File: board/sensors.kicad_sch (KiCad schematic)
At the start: 59 parts, among them J4 SWIM, U4 STM8S003F3P, U5 MAX-M8C, U6 LM324, U7 LM324

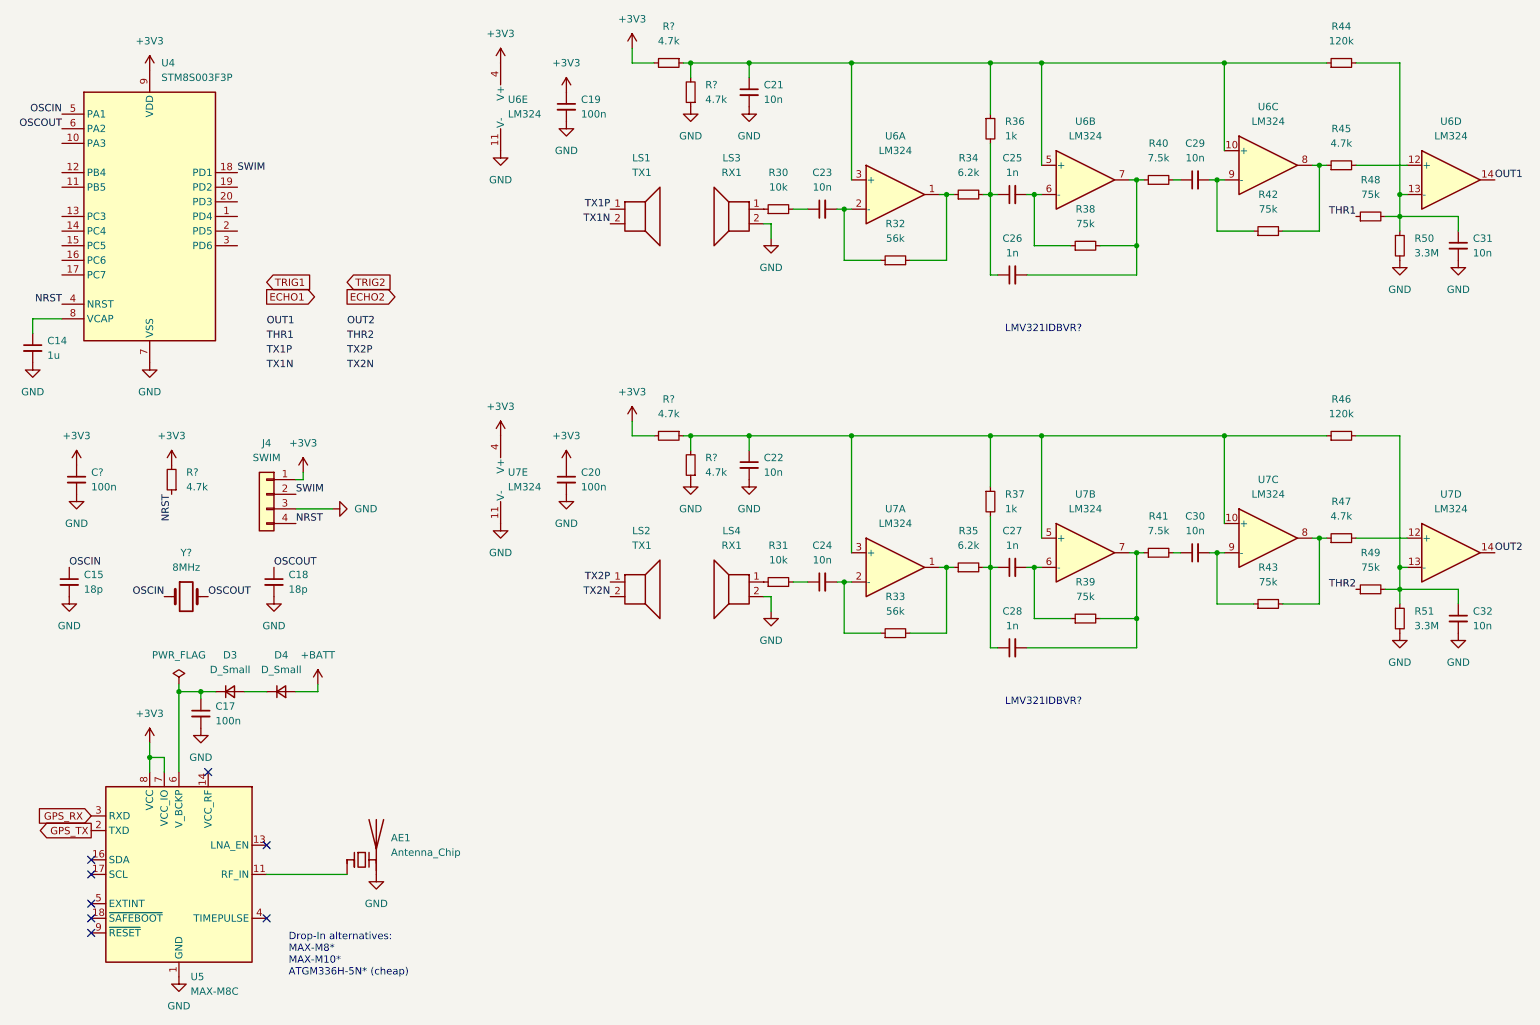
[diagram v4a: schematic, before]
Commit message: Added new ultrasonic circuit, changed the 3.3V regulator to a buck converter, and fixed some issues
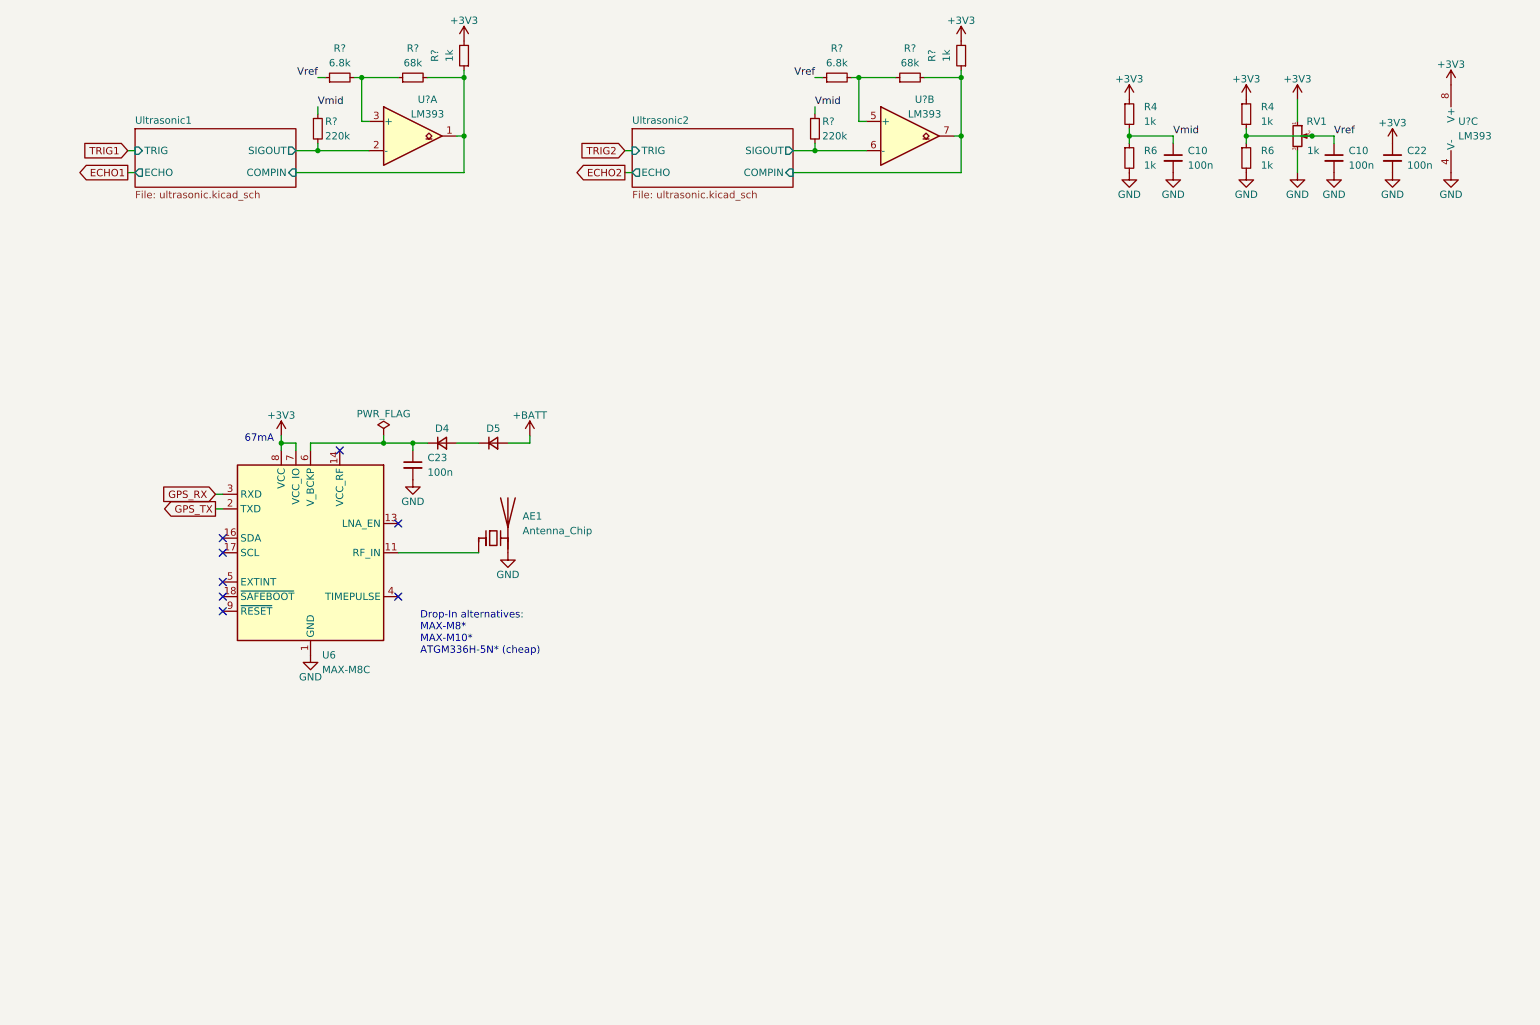
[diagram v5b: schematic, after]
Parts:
- removed C14: 1u, Capacitor_SMD:C_0603_1608Metric, symbol Device:C_Small
- removed C15, C18: 18p, Capacitor_SMD:C_0603_1608Metric, symbol Device:C_Small
- removed C19, C20, C?: 100n, Capacitor_SMD:C_0603_1608Metric, symbol Device:C_Small
- removed C21, C23, C24, C29, C30, C31, C32: 10n, Capacitor_SMD:C_0603_1608Metric, symbol Device:C_Small
- removed C25, C26, C27, C28: 1n, Capacitor_SMD:C_0603_1608Metric, symbol Device:C_Small
- removed J4: SWIM, symbol Connector_Generic:Conn_01x04
- removed LS1, LS2: TX1, symbol Device:Speaker
- removed LS3, LS4: RX1, symbol Device:Speaker
- removed R30, R31: 10k, Resistor_SMD:R_0603_1608Metric, symbol Device:R_Small
- removed R32, R33: 56k, Resistor_SMD:R_0603_1608Metric, symbol Device:R_Small
- removed R34, R35: 6.2k, Resistor_SMD:R_0603_1608Metric, symbol Device:R_Small
- removed R36, R37: 1k, Resistor_SMD:R_0603_1608Metric, symbol Device:R_Small
- removed R38, R39, R42, R43, R48, R49: 75k, Resistor_SMD:R_0603_1608Metric, symbol Device:R_Small
- removed R40, R41: 7.5k, Resistor_SMD:R_0603_1608Metric, symbol Device:R_Small
- removed R44, R46: 120k, Resistor_SMD:R_0603_1608Metric, symbol Device:R_Small
- removed R45, R47, R? (x5): 4.7k, Resistor_SMD:R_0603_1608Metric, symbol Device:R_Small
- removed R50, R51: 3.3M, Resistor_SMD:R_0603_1608Metric, symbol Device:R_Small
- removed U4: STM8S003F3P, Package_SO:TSSOP-20_4.4x6.5mm_P0.65mm, symbol MCU_ST_STM8:STM8S003F3P
- removed U6, U7: LM324, Package_SO:SOIC-14_3.9x8.7mm_P1.27mm, symbol Amplifier_Operational:LM324
- removed Y?: Crystal, symbol Device:Crystal
- added C10 (x2): 100n, Capacitor_SMD:C_0603_1608Metric_Pad1.08x0.95mm_HandSolder, symbol Device:C_Small
- added R4 (x2), R6 (x2), R? (x2): 1k, Resistor_SMD:R_0603_1608Metric, symbol Device:R_Small
- added R? (x2): 75k, Resistor_SMD:R_0603_1608Metric, symbol Device:R_Small
- added R? (x2): R_Small, Resistor_SMD:R_0603_1608Metric, symbol Device:R_Small
- added R? (x2): 3.3M, Resistor_SMD:R_0603_1608Metric, symbol Device:R_Small
- added RV1: 1k, Potentiometer_THT:Potentiometer_Bourns_3266W_Vertical, symbol Device:R_Potentiometer_Small
- added U? (x3): LM393, Package_SO:SOIC-8_3.9x4.9mm_P1.27mm, symbol Comparator:LM393
- AE1: footprint (none) -> OBSPro:GPS1003
- C22: value 10n -> 100n; footprint Capacitor_SMD:C_0603_1608Metric -> Capacitor_SMD:C_0603_1608Metric_Pad1.08x0.95mm_HandSolder; JLC_PN C57112 -> C14663; JLC_Price1 (none) -> 0.042; JLC_Price10 (none) -> 0.0042; JLC_Price100 (none) -> 0.0021; JLC_Price1000 (none) -> 0.0014; MPN 0603B103K500NT -> CC0603KRX7R9BB104; Manufacturer FH (Guangdong Fenghua Advanced Tech) -> YAGEO; kicost:JLC:pricing 1: USD 0.0012 -> (none)
- renumbered C17 to C23, D3 to D4, D4 to D5, U5 to U6
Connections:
- net +3V3: now also C22.1, R4.1, R4.1, R?.2, R?.2, RV1.1, U?.8 (V+)
- net GND: now also C10.2, C10.2, R6.2, R6.2, RV1.3, U?.4 (V-)
- new net: R?.1, R?.2, U?.5 (+)
- new net: R?.1, R?.2, U?.3 (+)
- new net Ultrasonic1/COMPIN: R?.1, R?.2, U?.1
- new net Ultrasonic1/SIGOUT: R?.2, U?.2 (-)
- new net Ultrasonic2/COMPIN: R?.1, R?.2, U?.7
- new net Ultrasonic2/SIGOUT: R?.2, U?.6 (-)
- new net Vmid: C10.1, R4.2, R6.1, R?.1, R?.1
- new net Vref: C10.1, R4.2, R6.1, R?.1, R?.1, RV1.2
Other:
- added sheet Ultrasonic1 (ultrasonic.kicad_sch)
- added sheet Ultrasonic2 (ultrasonic.kicad_sch)
- note added: "67mA"
- note removed: "LMV321IDBVR?"
- moved on the sheet: AE1, C23, D4, D5, U6

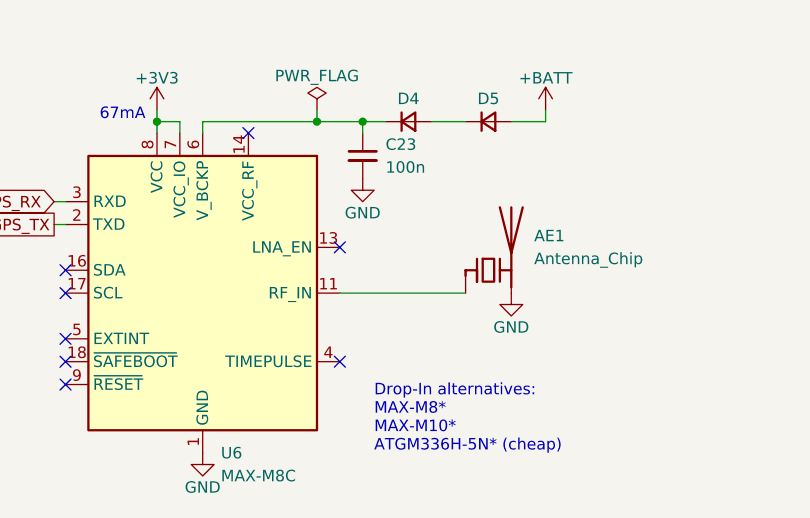
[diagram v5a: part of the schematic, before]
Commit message: First placement of parts, fixed a few bugs in the schematic
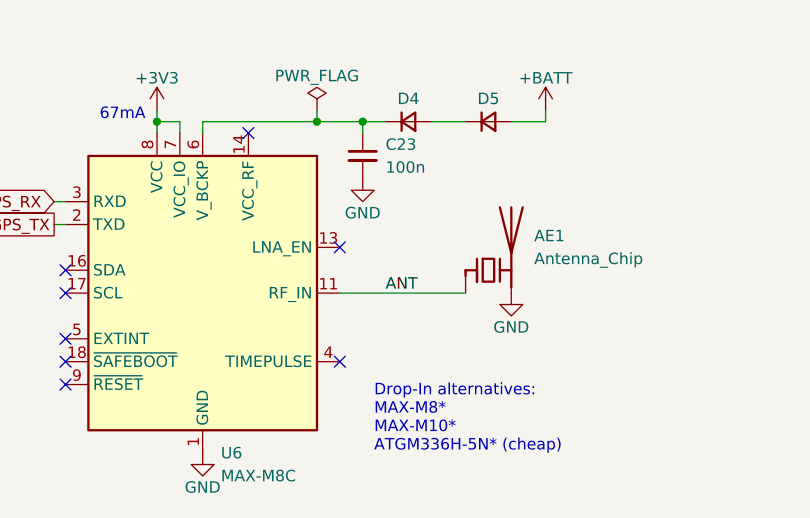
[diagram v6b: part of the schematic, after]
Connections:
- net ANT: now reaches AE1.1 (FEED), U6.11 (RF_IN)
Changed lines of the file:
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@@
+    (effects (font (size 1.27 1.27)) (justify left bottom))
+  )
+  (label "ANT" (at 87.63 115.57 0)
     (effects (font (size 1.27 1.27)) (justify left bottom))
   )
@@
   (symbol (lib_id "power:GND") (at 85.09 102.87 0) (unit 1)
     (in_bom yes) (on_board yes) (fields_autoplaced)
-    (property "Reference" "#PWR0152" (id 0) (at 85.09 109.22 0)
+    (property "Reference" "#PWR082" (id 0) (at 85.09 109.22 0)
       (effects (font (size 1.27 1.27)) hide)
     )
@@
   (symbol (lib_id "power:+3V3") (at 93.98 26.67 0) (unit 1)
     (in_bom yes) (on_board yes) (fields_autoplaced)
-    (property "Reference" "#PWR0201" (id 0) (at 93.98 30.48 0)
+    (property "Reference" "#PWR066" (id 0) (at 93.98 30.48 0)
       (effects (font (size 1.27 1.27)) hide)
     )
@@
   (symbol (lib_id "power:+3V3") (at 238.76 36.83 0) (unit 1)
     (in_bom yes) (on_board yes) (fields_autoplaced)
-    (property "Reference" "#PWR0205" (id 0) (at 238.76 40.64 0)
+    (property "Reference" "#PWR071" (id 0) (at 238.76 40.64 0)
       (effects (font (size 1.27 1.27)) hide)
     )
@@
   (symbol (lib_id "power:GND") (at 265.43 49.53 0) (unit 1)
     (in_bom yes) (on_board yes) (fields_autoplaced)
-    (property "Reference" "#PWR0159" (id 0) (at 265.43 55.88 0)
+    (property "Reference" "#PWR079" (id 0) (at 265.43 55.88 0)
       (effects (font (size 1.27 1.27)) hide)
     )
@@
   (symbol (lib_id "power:GND") (at 238.76 49.53 0) (unit 1)
     (in_bom yes) (on_board yes) (fields_autoplaced)
-    (property "Reference" "#PWR0157" (id 0) (at 238.76 55.88 0)
+    (property "Reference" "#PWR076" (id 0) (at 238.76 55.88 0)
       (effects (font (size 1.27 1.27)) hide)
     )
@@
   (symbol (lib_id "power:+3V3") (at 255.27 44.45 0) (unit 1)
     (in_bom yes) (on_board yes) (fields_autoplaced)
-    (property "Reference" "#PWR0225" (id 0) (at 255.27 48.26 0)
+    (property "Reference" "#PWR072" (id 0) (at 255.27 48.26 0)
       (effects (font (size 1.27 1.27)) hide)
     )
@@
   (symbol (lib_id "power:GND") (at 229.87 49.53 0) (unit 1)
     (in_bom yes) (on_board yes) (fields_autoplaced)
-    (property "Reference" "#PWR0156" (id 0) (at 229.87 55.88 0)
+    (property "Reference" "#PWR075" (id 0) (at 229.87 55.88 0)
       (effects (font (size 1.27 1.27)) hide)
     )
@@
   (symbol (lib_id "power:+3V3") (at 62.23 95.25 0) (unit 1)
     (in_bom yes) (on_board yes) (fields_autoplaced)
-    (property "Reference" "#PWR0203" (id 0) (at 62.23 99.06 0)
+    (property "Reference" "#PWR080" (id 0) (at 62.23 99.06 0)
       (effects (font (size 1.27 1.27)) hide)
     )
@@
   (symbol (lib_id "power:GND") (at 67.31 133.35 0) (unit 1)
     (in_bom yes) (on_board yes) (fields_autoplaced)
-    (property "Reference" "#PWR0151" (id 0) (at 67.31 139.7 0)
+    (property "Reference" "#PWR084" (id 0) (at 67.31 139.7 0)
       (effects (font (size 1.27 1.27)) hide)
     )
@@
   (symbol (lib_id "power:GND") (at 255.27 49.53 0) (unit 1)
     (in_bom yes) (on_board yes) (fields_autoplaced)
-    (property "Reference" "#PWR0158" (id 0) (at 255.27 55.88 0)
+    (property "Reference" "#PWR078" (id 0) (at 255.27 55.88 0)
       (effects (font (size 1.27 1.27)) hide)
     )
@@
   (symbol (lib_id "power:GND") (at 101.6 115.57 0) (unit 1)
     (in_bom yes) (on_board yes) (fields_autoplaced)
-    (property "Reference" "#PWR0153" (id 0) (at 101.6 121.92 0)
+    (property "Reference" "#PWR083" (id 0) (at 101.6 121.92 0)
       (effects (font (size 1.27 1.27)) hide)
     )
@@
   (symbol (lib_id "power:GND") (at 217.17 49.53 0) (unit 1)
     (in_bom yes) (on_board yes) (fields_autoplaced)
-    (property "Reference" "#PWR0155" (id 0) (at 217.17 55.88 0)
+    (property "Reference" "#PWR074" (id 0) (at 217.17 55.88 0)
       (effects (font (size 1.27 1.27)) hide)
     )
@@
   (symbol (lib_id "power:+3V3") (at 229.87 36.83 0) (unit 1)
     (in_bom yes) (on_board yes) (fields_autoplaced)
-    (property "Reference" "#PWR0206" (id 0) (at 229.87 40.64 0)
+    (property "Reference" "#PWR070" (id 0) (at 229.87 40.64 0)
       (effects (font (size 1.27 1.27)) hide)
     )
@@
   (symbol (lib_id "power:GND") (at 245.11 49.53 0) (unit 1)
     (in_bom yes) (on_board yes) (fields_autoplaced)
-    (property "Reference" "#PWR0160" (id 0) (at 245.11 55.88 0)
+    (property "Reference" "#PWR077" (id 0) (at 245.11 55.88 0)
       (effects (font (size 1.27 1.27)) hide)
     )
@@
   (symbol (lib_id "power:+BATT") (at 105.41 95.25 0) (unit 1)
     (in_bom yes) (on_board yes) (fields_autoplaced)
-    (property "Reference" "#PWR0204" (id 0) (at 105.41 99.06 0)
+    (property "Reference" "#PWR081" (id 0) (at 105.41 99.06 0)
       (effects (font (size 1.27 1.27)) hide)
     )
@@
   (symbol (lib_id "power:+3V3") (at 180.34 26.67 0) (unit 1)
     (in_bom yes) (on_board yes) (fields_autoplaced)
-    (property "Reference" "#PWR0202" (id 0) (at 180.34 30.48 0)
+    (property "Reference" "#PWR067" (id 0) (at 180.34 30.48 0)
       (effects (font (size 1.27 1.27)) hide)
     )
@@
   (symbol (lib_id "power:+3V3") (at 265.43 34.29 0) (unit 1)
     (in_bom yes) (on_board yes) (fields_autoplaced)
-    (property "Reference" "#PWR0208" (id 0) (at 265.43 38.1 0)
+    (property "Reference" "#PWR068" (id 0) (at 265.43 38.1 0)
       (effects (font (size 1.27 1.27)) hide)
     )
@@
   (symbol (lib_id "power:GND") (at 209.55 49.53 0) (unit 1)
     (in_bom yes) (on_board yes) (fields_autoplaced)
-    (property "Reference" "#PWR0154" (id 0) (at 209.55 55.88 0)
+    (property "Reference" "#PWR073" (id 0) (at 209.55 55.88 0)
       (effects (font (size 1.27 1.27)) hide)
     )
@@
   (symbol (lib_id "power:+3V3") (at 209.55 36.83 0) (unit 1)
     (in_bom yes) (on_board yes) (fields_autoplaced)
-    (property "Reference" "#PWR0207" (id 0) (at 209.55 40.64 0)
+    (property "Reference" "#PWR069" (id 0) (at 209.55 40.64 0)
       (effects (font (size 1.27 1.27)) hide)
     )
@@
   (symbol (lib_id "power:PWR_FLAG") (at 80.01 95.25 0) (unit 1)
     (in_bom yes) (on_board yes)
-    (property "Reference" "#FLG0104" (id 0) (at 80.01 93.345 0)
-      (effects (font (size 1.27 1.27)) hide)
-    )
+    (property "Reference" "#FLG05" (id 0) (at 80.01 93.345 0)
+      (effects (font (size 1.27 1.27)) hide)
+    )

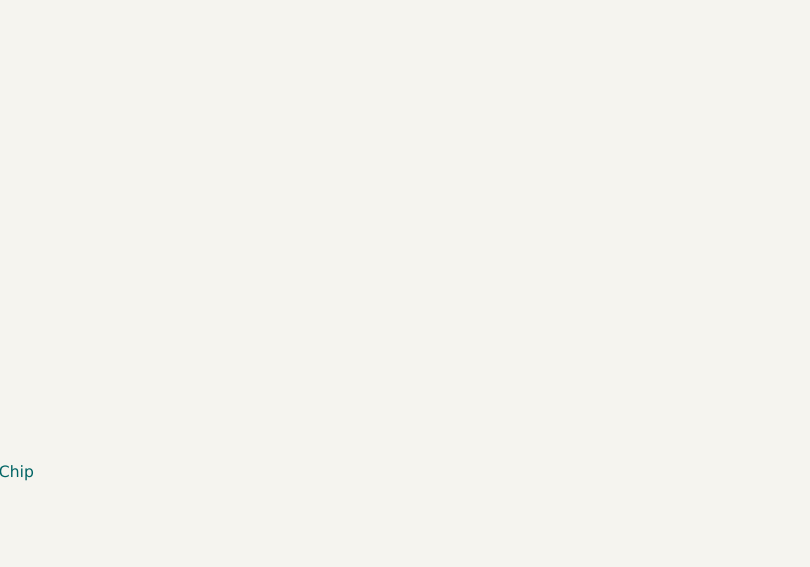
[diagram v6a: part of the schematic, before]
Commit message: Swapped footprints of connectors, optimized placement
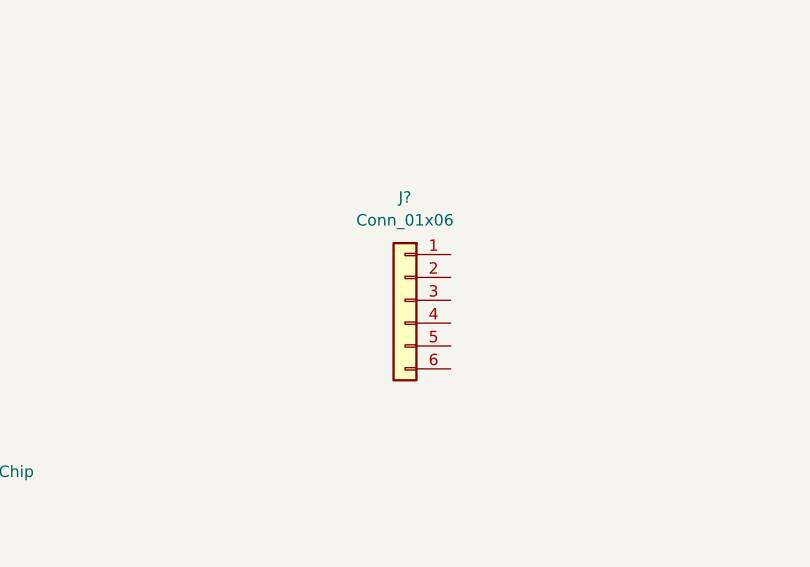
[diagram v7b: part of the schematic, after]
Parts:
- added J?: Conn_01x06, symbol Connector_Generic:Conn_01x06
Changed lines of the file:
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@@
     (pin "1")
+  )
+  (symbol (lib_id "Connector_Generic:Conn_01x06") (at 157.48 92.71 0) (mirror y) (unit 1)
+    (in_bom yes) (on_board yes) (fields_autoplaced)
+    (property "Reference" "J?" (id 0) (at 157.48 81.28 0))
+    (property "Value" "Conn_01x06" (id 1) (at 157.48 83.82 0))
+    (property "Footprint" "" (id 2) (at 157.48 92.71 0)
+      (effects (font (size 1.27 1.27)) hide)
+    )
+    (property "Datasheet" "~" (id 3) (at 157.48 92.71 0)
+      (effects (font (size 1.27 1.27)) hide)
+    )
+    (pin "1")
+    (pin "2")
+    (pin "3")
+    (pin "4")
+    (pin "5")
+    (pin "6")
   )
   (symbol (lib_id "Device:R_Small") (at 68.58 41.91 0) (unit 1)
